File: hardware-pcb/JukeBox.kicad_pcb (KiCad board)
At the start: 2 copper layers, 90 x 90 mm, 79 parts, among them J1 USB4105-GF-A, J2 AudioJack4_Ground, Q1 Q_NPN_ECB, SW1 SW_SPST, SW10 SW_SPST, SW11 SW_SPST, SW12 SW_SPST, SW2 SW_SPST, SW3 SW_SPST, SW4 SW_SPST, SW5 SW_SPST, SW6 SW_SPST, SW7 SW_SPST, SW8 SW_SPST, SW9 SW_SPST, U1 NCP1117-3.3_SOT223, U2 W25Q128JVS, U3 RP2040, U4 st7789v, Y1 ECS-120-20-33-AEL-TR

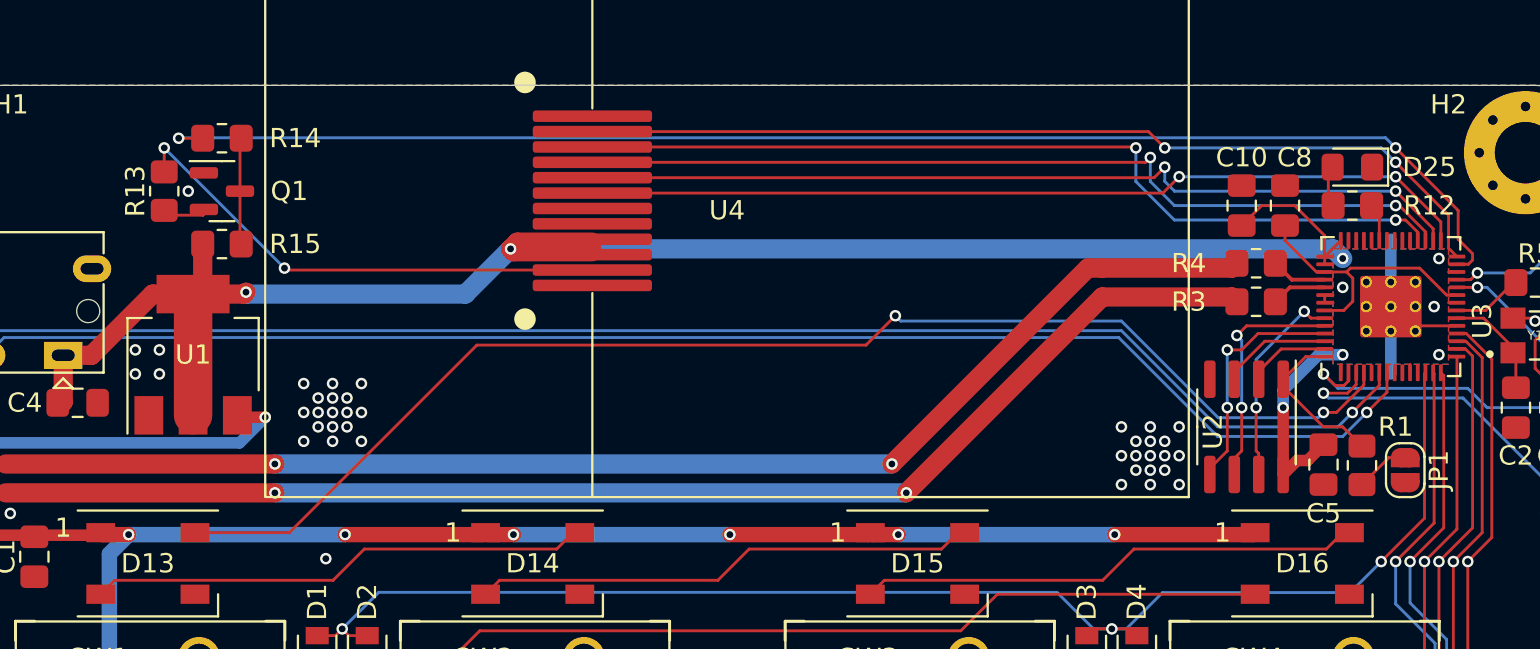
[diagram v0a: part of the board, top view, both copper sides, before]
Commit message: update flash chip, fix backlight transistor, adjust some holes for io, update readme for hardware
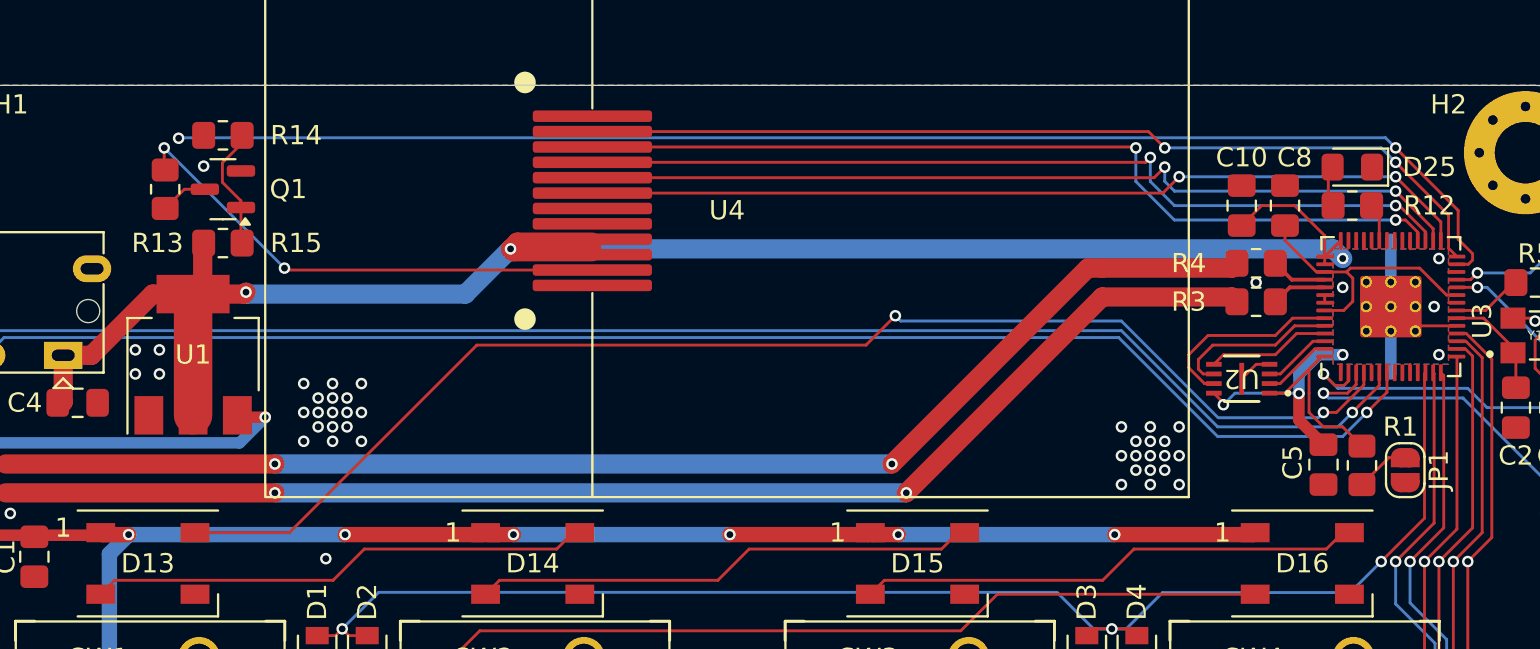
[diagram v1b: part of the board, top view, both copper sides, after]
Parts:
- D1, D10, D11, D12, D2, D3, D4, D5, D6, D7, D8, D9: value type="D" model="DIODE" lib="" -> 1N4148W
- Q1: value Q_NPN_ECB -> Q_NPN_BEC
- U2: value W25Q128JVS -> W25Q16JVUXIQ TR; footprint Package_SO:SOIC-8_3.9x4.9mm_P1.27mm -> JukeBox:USON-8_UX_2x3x0p6_WIN
- moved U2 2.51 mm to (139.3, 92.2), turned to 180 degrees
- moved R14 0.16 mm to (86.4, 79.6)
- moved Q1 0.11 mm to (86.4, 82.4), turned to 180 degrees
- moved R13 0.11 mm to (83.4, 82.4)
- moved R15 0.07 mm to (86.4, 85.2)
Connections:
- Q1 pad 1: GND -> Net-(Q1-B)
- Q1 pad 2: Net-(Q1-C) -> GND
- Q1 pad 3: Net-(Q1-B) -> Net-(Q1-C)
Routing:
- net /QSPI_SD0: track 12.3 -> 6.42 mm, vias 2 -> 0
- net /QSPI_SCLK: track 12.3 -> 8.70 mm, vias 2 -> 0
- net /QSPI_SD2: track 5.74 -> 3.57 mm
- net GND: track 33.2 -> 34.9 mm, vias 64 -> 65
- net /GPIO16: track 73.1 -> 71.9 mm
- net /QSPI_SS: track 8.40 -> 9.38 mm
- net Net-(Q1-B): track 5.55 -> 6.45 mm
- net +3V3: track 113.3 -> 114.1 mm, vias 9 -> 10
- net /QSPI_SD1: track 4.32 -> 3.61 mm
- net /QSPI_SD3: track 10.8 -> 10.2 mm, vias 2 -> 0

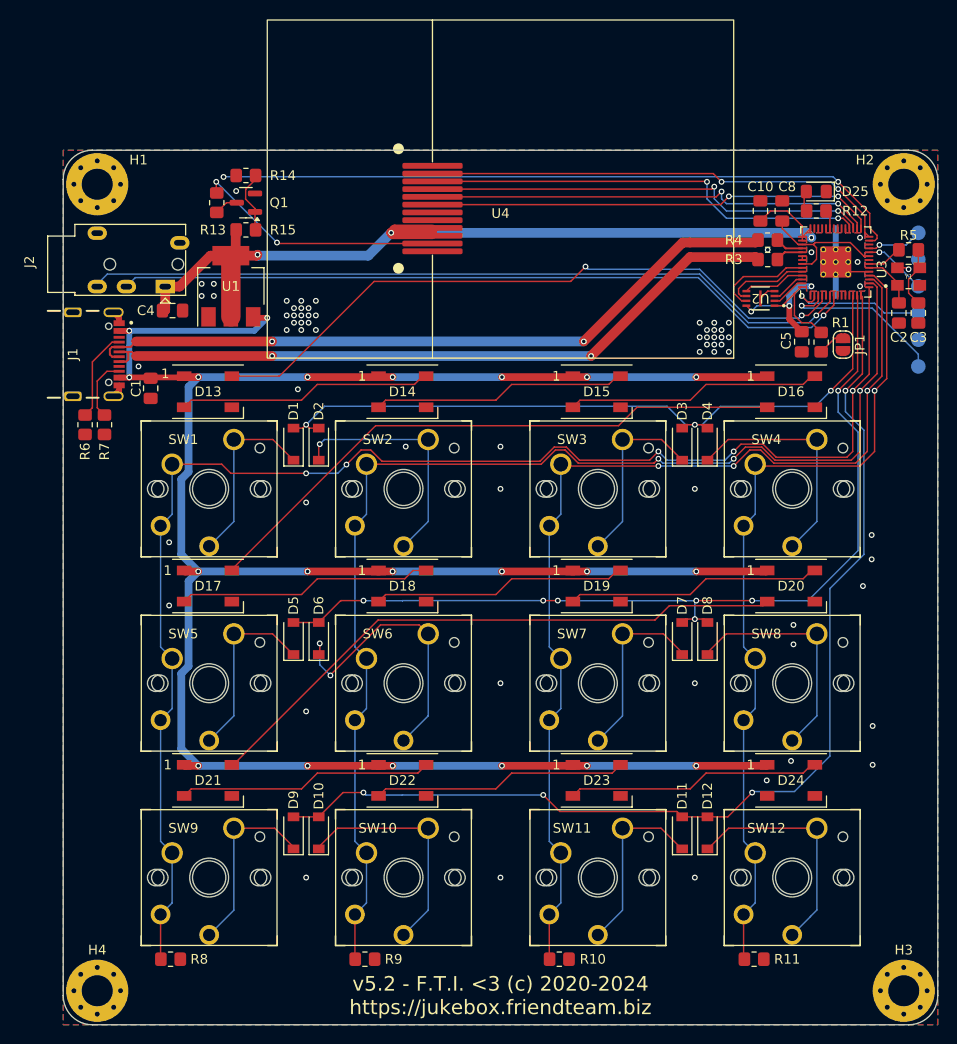
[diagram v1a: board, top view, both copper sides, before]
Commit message: remove headphone jack, switch to test pads, use 2020 leds and rearrange, move usb port
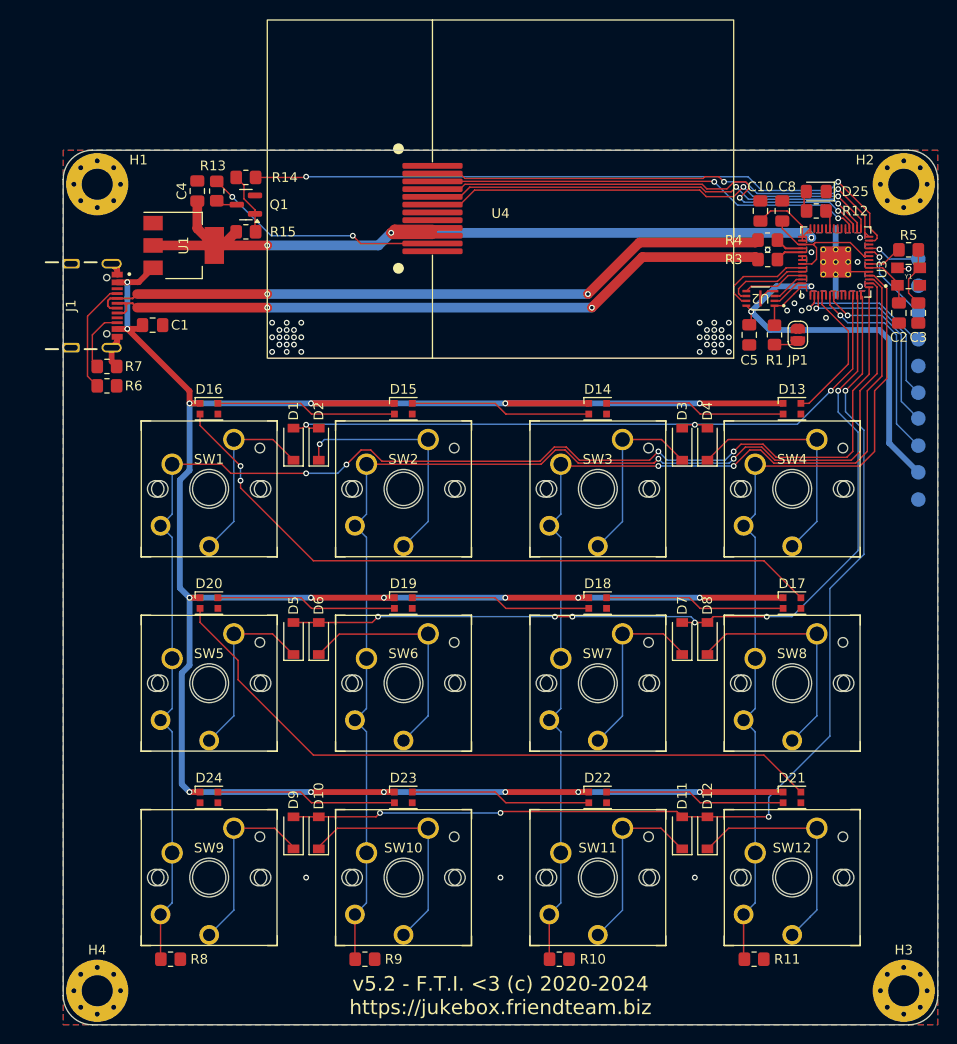
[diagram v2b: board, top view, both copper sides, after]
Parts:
- removed J2: AudioJack4_Ground, Connector_Audio:Jack_3.5mm_PJ320E_Horizontal
- added TP31: TestPoint, TestPoint:TestPoint_Pad_D1.5mm, B.Cu at (155.6, 107.4)
- added TP32: TestPoint, TestPoint:TestPoint_Pad_D1.5mm, B.Cu at (155.6, 104.6)
- added TP33: TestPoint, TestPoint:TestPoint_Pad_D1.5mm, B.Cu at (155.6, 110.2)
- added TP34: TestPoint, TestPoint:TestPoint_Pad_D1.5mm, B.Cu at (155.6, 113.0)
- D13, D14, D15, D16, D17, D18, D19, D20, D21, D22, D23, D24: footprint LED_SMD:LED_WS2812B_PLCC4_5.0x5.0mm_P3.2mm -> LED_SMD:LED_WS2812B-2020_PLCC4_2.0x2.0mm
- moved D13 60.1 mm to (142.6, 103.6)
- moved D17 60.1 mm to (142.6, 123.6)
- moved D21 60.1 mm to (142.6, 143.6)
- moved D16 59.9 mm to (82.6, 103.6)
- moved D20 59.9 mm to (82.6, 123.6)
- moved D24 59.9 mm to (82.6, 143.6)
- moved D14 20.2 mm to (122.6, 103.6)
- moved D18 20.2 mm to (122.6, 123.6)
- moved D22 20.2 mm to (122.6, 143.6)
- moved D15 20.0 mm to (102.6, 103.6)
- moved D19 20.0 mm to (102.6, 123.6)
- moved D23 20.0 mm to (102.6, 143.6)
- moved C4 12.6 mm to (81.4, 81.2), turned to 90 degrees
- moved C1 6.50 mm to (76.8, 95.0), turned to 0 degrees
- moved U1 6.42 mm to (80.0, 86.8), turned to 0 degrees
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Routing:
- net /GPIO5: track 77.3 -> 18.3 mm
- net /GPIO4: track 79.5 -> 21.4 mm
- net /GPIO2: track 69.1 -> 14.7 mm, vias 2 -> 0
- net +3V3: track 114.1 -> 138.2 mm, vias 10 -> 9
- net VBUS: track 253.6 -> 271.7 mm, vias 21 -> 18
- net Net-(D20-DOUT): track 62.1 -> 71.7 mm
- net Net-(D16-DOUT): track 62.1 -> 71.7 mm, vias 0 -> 2
- net Net-(D22-DOUT): track 26.2 -> 18.6 mm
- net Net-(D23-DOUT): track 26.2 -> 18.6 mm
- net Net-(D19-DOUT): track 26.2 -> 18.6 mm
- net Net-(D15-DOUT): track 26.2 -> 18.6 mm
- net Net-(D14-DOUT): track 26.2 -> 18.6 mm
- net Net-(D18-DOUT): track 26.2 -> 18.6 mm
- net Net-(D21-DOUT): track 26.2 -> 18.6 mm
- net Net-(D17-DOUT): track 26.2 -> 18.6 mm
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
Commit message: switch to 2020 leds, switch to new key footprint, extend io connectors, update case geometry
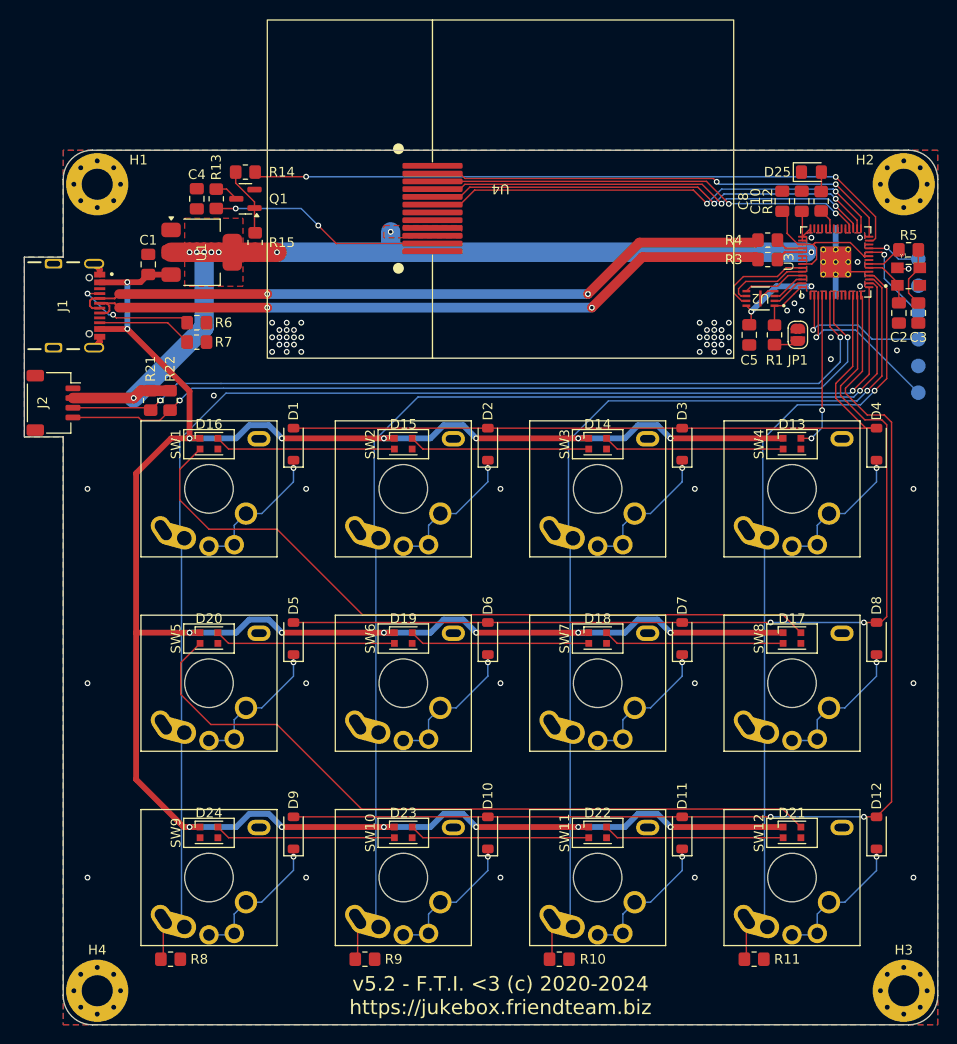
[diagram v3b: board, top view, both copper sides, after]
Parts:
- removed TP31, TP32, TP33, TP34: TestPoint, TestPoint:TestPoint_Pad_D1.5mm
- added J2: Conn_01x04_Pin, Connector_JST:JST_SH_SM04B-SRSS-TB_1x04-1MP_P1.00mm_Horizontal, F.Cu at (66.6, 103.0)
- added R21: 2k, Resistor_SMD:R_0805_2012Metric_Pad1.20x1.40mm_HandSolder, F.Cu at (76.6, 102.8)
- added R22: 2k, Resistor_SMD:R_0805_2012Metric_Pad1.20x1.40mm_HandSolder, F.Cu at (78.6, 102.8)
- J1: footprint RP2040_minimal:GCT_USB4105-GF-A -> JukeBox:GCT_USB4105-GF-A
- R12: value 200 -> 600
- SW1, SW10, SW11, SW12, SW2, SW3, SW4, SW5, SW6, SW7, SW8, SW9: footprint RP2040_minimal:Kailh_Choc_MX_Key -> JukeBox:ALLKEY
- U3: footprint RP2040_minimal:RP2040-QFN-56 -> JukeBox:RP2040-QFN-56
- U4: footprint RP2040_minimal:st7789v -> JukeBox:st7789v
- Y1: footprint RP2040_minimal:XTAL_ECS-120-20-33-AEL-TR -> JukeBox:XTAL_ECS-120-20-33-AEL-TR
- moved D10 17.4 mm to (111.3, 147.2)
- moved D12 17.4 mm to (151.3, 147.2)
- moved D2 17.4 mm to (111.3, 107.2)
- moved D4 17.4 mm to (151.3, 107.2)
- moved D6 17.4 mm to (111.3, 127.2)
- moved D8 17.4 mm to (151.3, 127.2)
- moved R6 11.3 mm to (81.3, 94.8)
- moved R7 9.58 mm to (81.3, 96.8)
- moved C1 6.27 mm to (76.3, 88.8), turned to 90 degrees
- moved C10 4.37 mm to (143.6, 82.2)
- moved D13 3.60 mm to (142.6, 107.2)
- moved D14 3.60 mm to (122.6, 107.2)
- moved D15 3.60 mm to (102.6, 107.2)
- moved D16 3.60 mm to (82.6, 107.2)
- moved D17 3.60 mm to (142.6, 127.2)
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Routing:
- net /GPIO5: track 18.3 -> 89.8 mm, vias 1 -> 2
- net /GPIO4: track 21.4 -> 88.4 mm, vias 1 -> 2
- net +3V3: track 138.2 -> 114.3 mm, vias 9 -> 15
- net VBUS: track 271.7 -> 283.9 mm, vias 18 -> 20
- net Net-(D2-A): track 25.1 -> 14.8 mm
- net Net-(D8-A): track 24.3 -> 14.8 mm, vias 0 -> 1
- net Net-(D10-A): track 24.3 -> 14.8 mm, vias 0 -> 1
- net /GPIO11: track 108.7 -> 118.1 mm, vias 4 -> 2
- net Net-(D4-A): track 24.2 -> 14.8 mm, vias 0 -> 1
- net Net-(D12-A): track 24.2 -> 14.8 mm, vias 0 -> 1
- net Net-(D6-A): track 24.2 -> 14.8 mm, vias 0 -> 1
- net /GPIO12: track 146.3 -> 137.8 mm, vias 4 -> 1
- net /GPIO10: track 91.0 -> 98.1 mm, vias 6 -> 2
- net /GPIO13: track 126.0 -> 119.4 mm, vias 2 -> 1
- net /GPIO14: track 105.9 -> 100.7 mm, vias 2 -> 1
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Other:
- board size 90 x 90 mm -> 94 x 90 mm

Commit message: remove old cad files, switch to 8MB flash
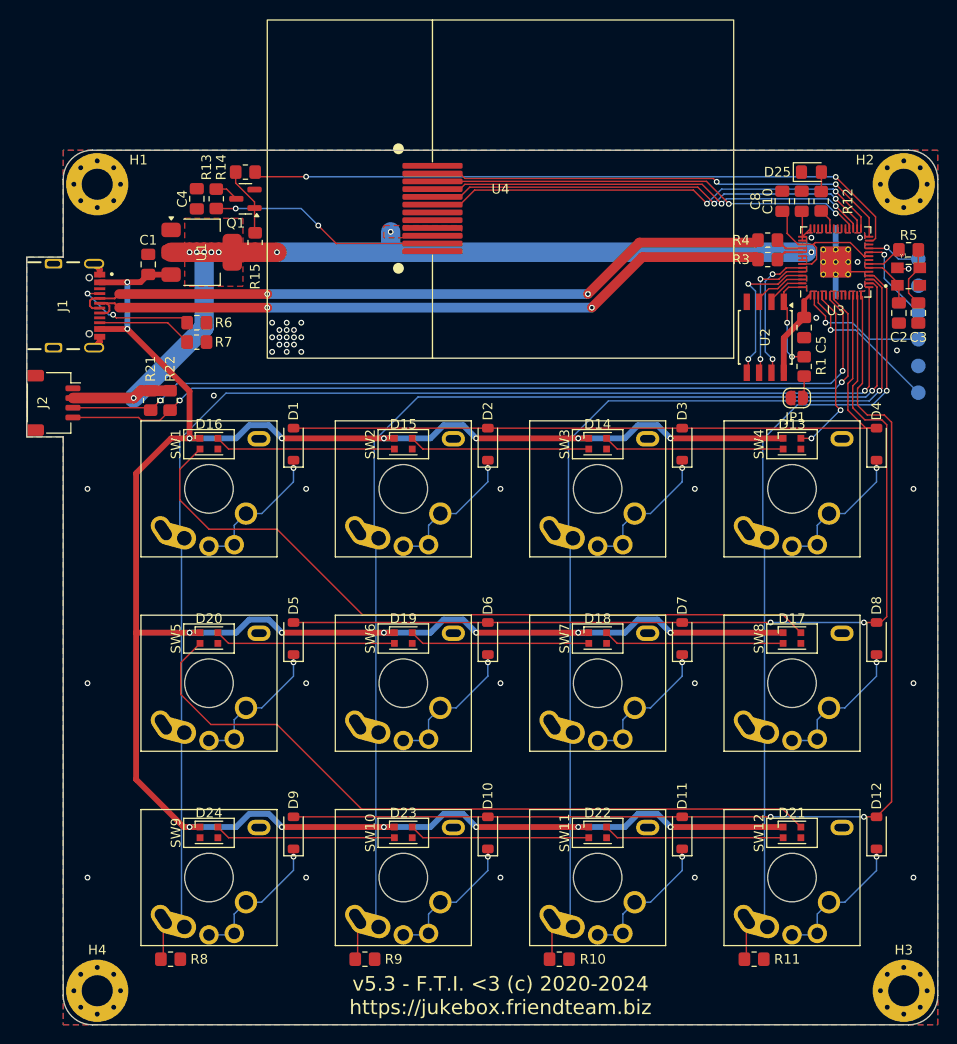
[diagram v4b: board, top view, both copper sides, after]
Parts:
- G***: footprint RP2040_minimal:FTI -> JukeBox:FTI
- G1: footprint RP2040_minimal:JukeBox -> JukeBox:JukeBox
- U2: value W25Q16JVUXIQ TR -> W25Q64JVSSIQ-TR; footprint JukeBox:USON-8_UX_2x3x0p6_WIN -> Package_SO:SOIC-8W_5.3x5.3mm_P1.27mm
- moved JP1 6.50 mm to (143.1, 102.5), turned to 0 degrees
- moved C5 5.70 mm to (143.8, 95.2)
- moved R1 4.46 mm to (143.8, 99.2)
- moved U2 4.03 mm to (139.8, 96.2), turned to -90 degrees
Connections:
- J2 pad MP: (no net) -> GND
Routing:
- net /QSPI_SD0: track 6.42 -> 15.8 mm, vias 0 -> 2
- net /QSPI_SCLK: track 8.70 -> 14.3 mm, vias 0 -> 2
- net /QSPI_SS: track 5.65 -> 10.4 mm, vias 0 -> 2
- net /QSPI_SD3: track 10.2 -> 14.2 mm, vias 0 -> 2
- net /DBGTX: track 17.9 -> 15.8 mm
- net /QSPI_SD2: track 3.57 -> 5.61 mm
- net GND: track 34.9 -> 33.1 mm, vias 58 -> 36
- net /DBGRX: track 15.2 -> 13.5 mm
- net /GPIO2: track 16.3 -> 17.9 mm
- net /GPIO9: track 76.8 -> 75.8 mm
- net /GPIO11: track 118.1 -> 117.0 mm
- net /GPIO10: track 98.1 -> 97.1 mm
- net /GPIO4: track 88.4 -> 89.4 mm
- net /GPIO5: track 89.8 -> 90.7 mm
- net /GPIO12: track 137.8 -> 138.5 mm
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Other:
- board size 94 x 90 mm -> 93.8 x 90 mm
- board text added: "v5.3 - F.T.I. <3 (c) 2020-2024 https://jukebox.friendteam.biz"
- board text removed: "v5.2 - F.T.I. <3 (c) 2020-2024 https://jukebox.friendteam.biz"

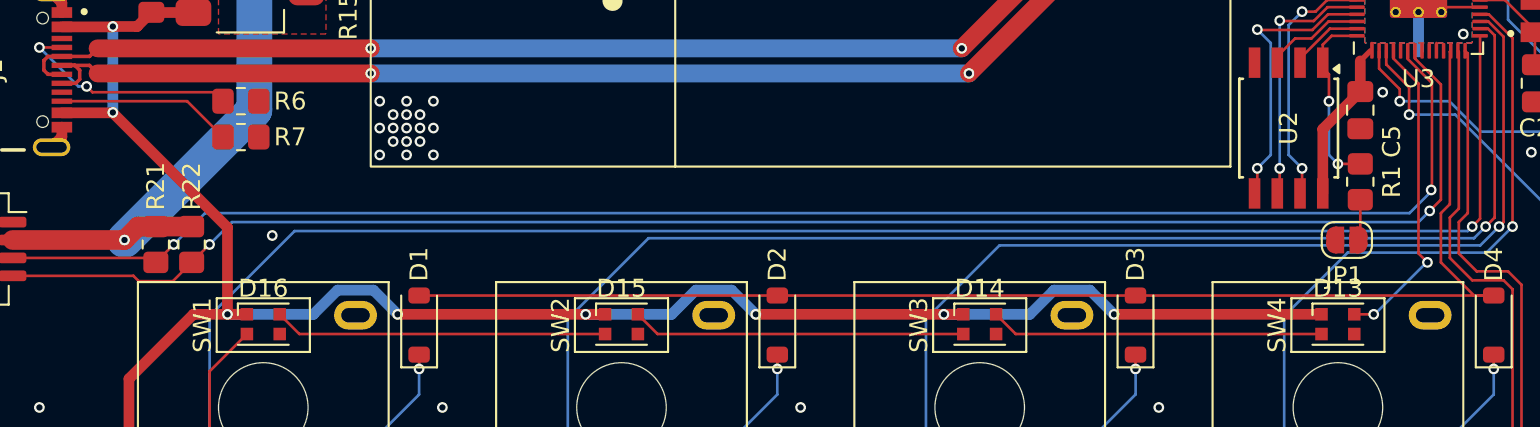
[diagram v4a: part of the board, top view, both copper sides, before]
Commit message: add eeprom for configuring the device persistently
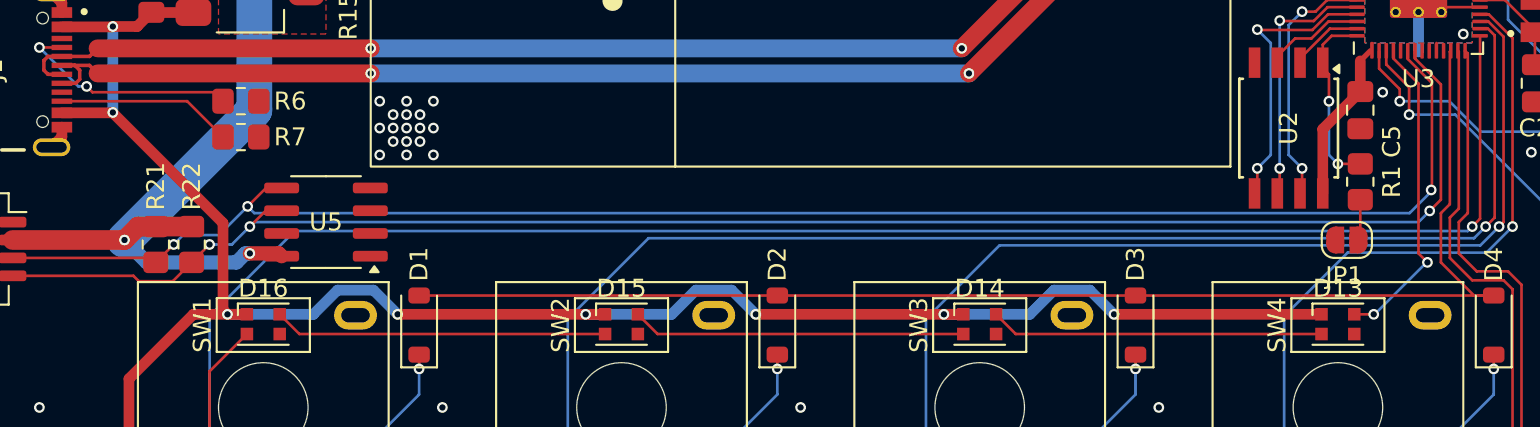
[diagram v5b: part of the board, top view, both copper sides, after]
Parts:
- added U5: CAT24C512, Package_SO:SOIC-8_3.9x4.9mm_P1.27mm, F.Cu at (86.1, 101.5)
- C2, C3: value 32p -> 27p
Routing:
- net +3V3: track 113.9 -> 123.4 mm, vias 13 -> 14
- net /GPIO4: track 89.4 -> 92.0 mm, vias 2 -> 3
- net /GPIO5: track 90.7 -> 92.8 mm, vias 2 -> 3
- net GND: vias 36 -> 35
